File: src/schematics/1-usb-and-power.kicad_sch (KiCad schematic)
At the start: 49 parts, among them Q101 NX6008NBKW, U101 MP5016HGQH, U102 BQ24392RSER, U103 FUSB302BMPX, U104 TPS628512DRLR

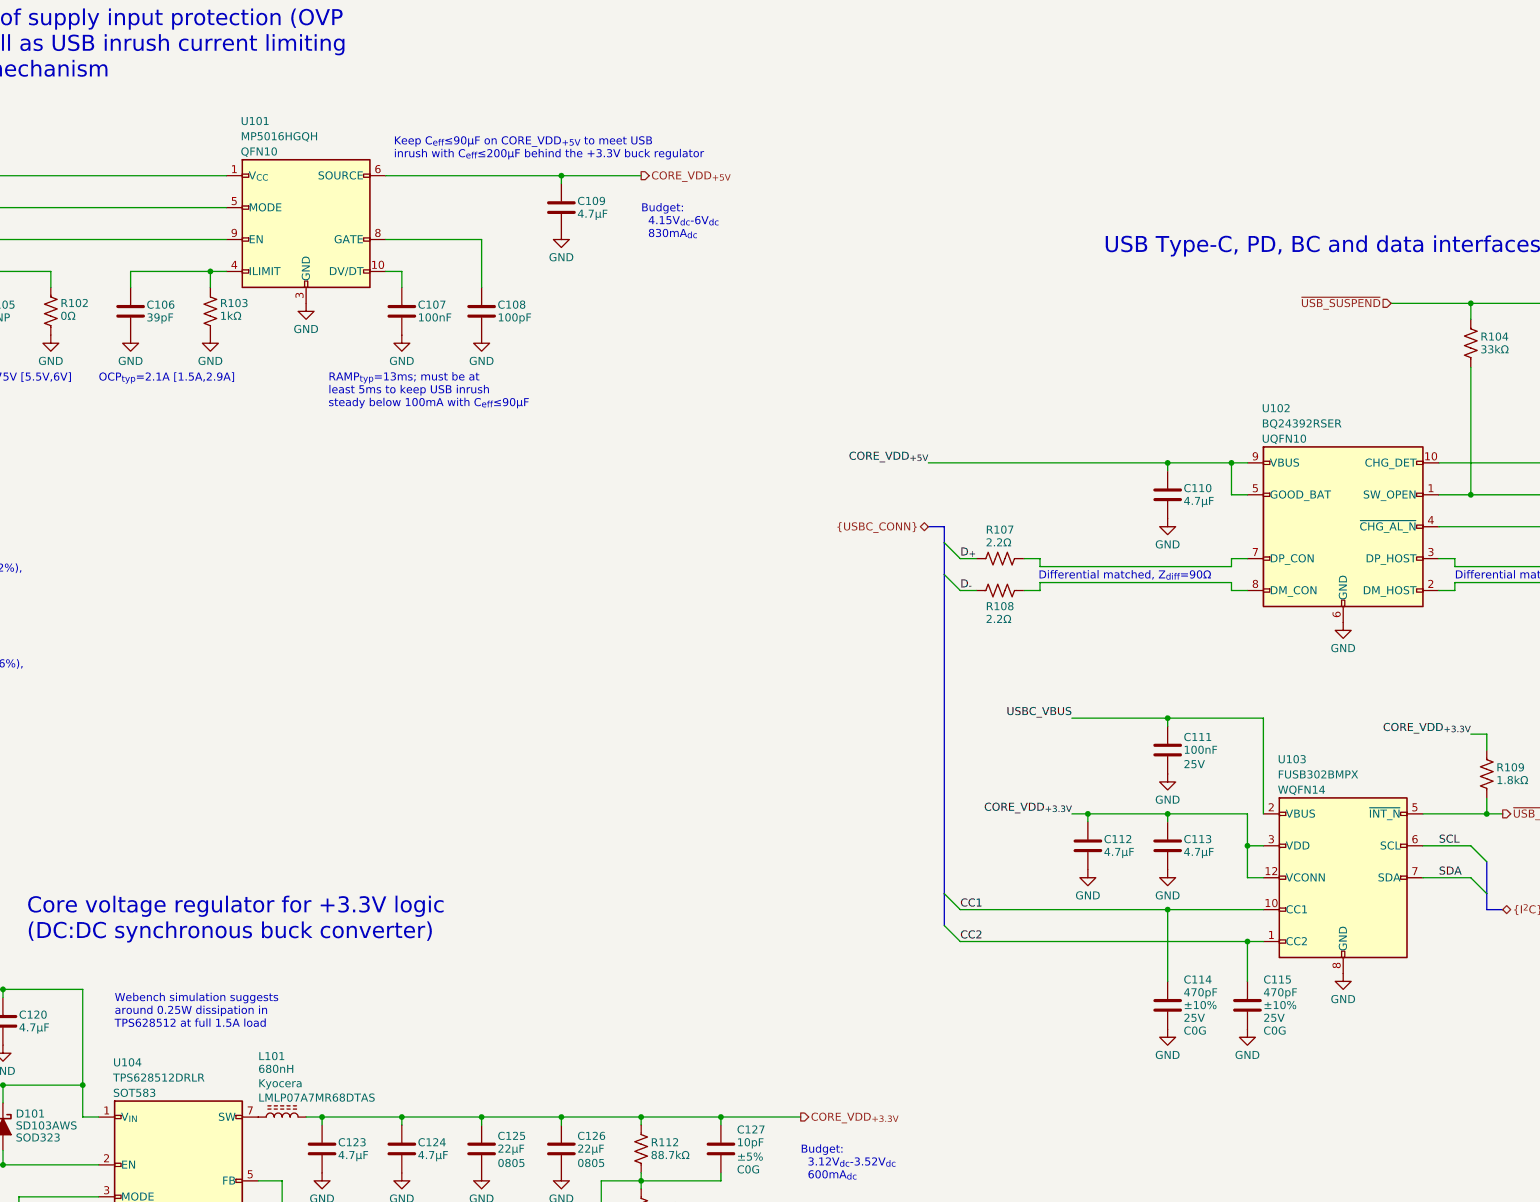
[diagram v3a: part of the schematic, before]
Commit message: Added the I2C address of the FUSB302.
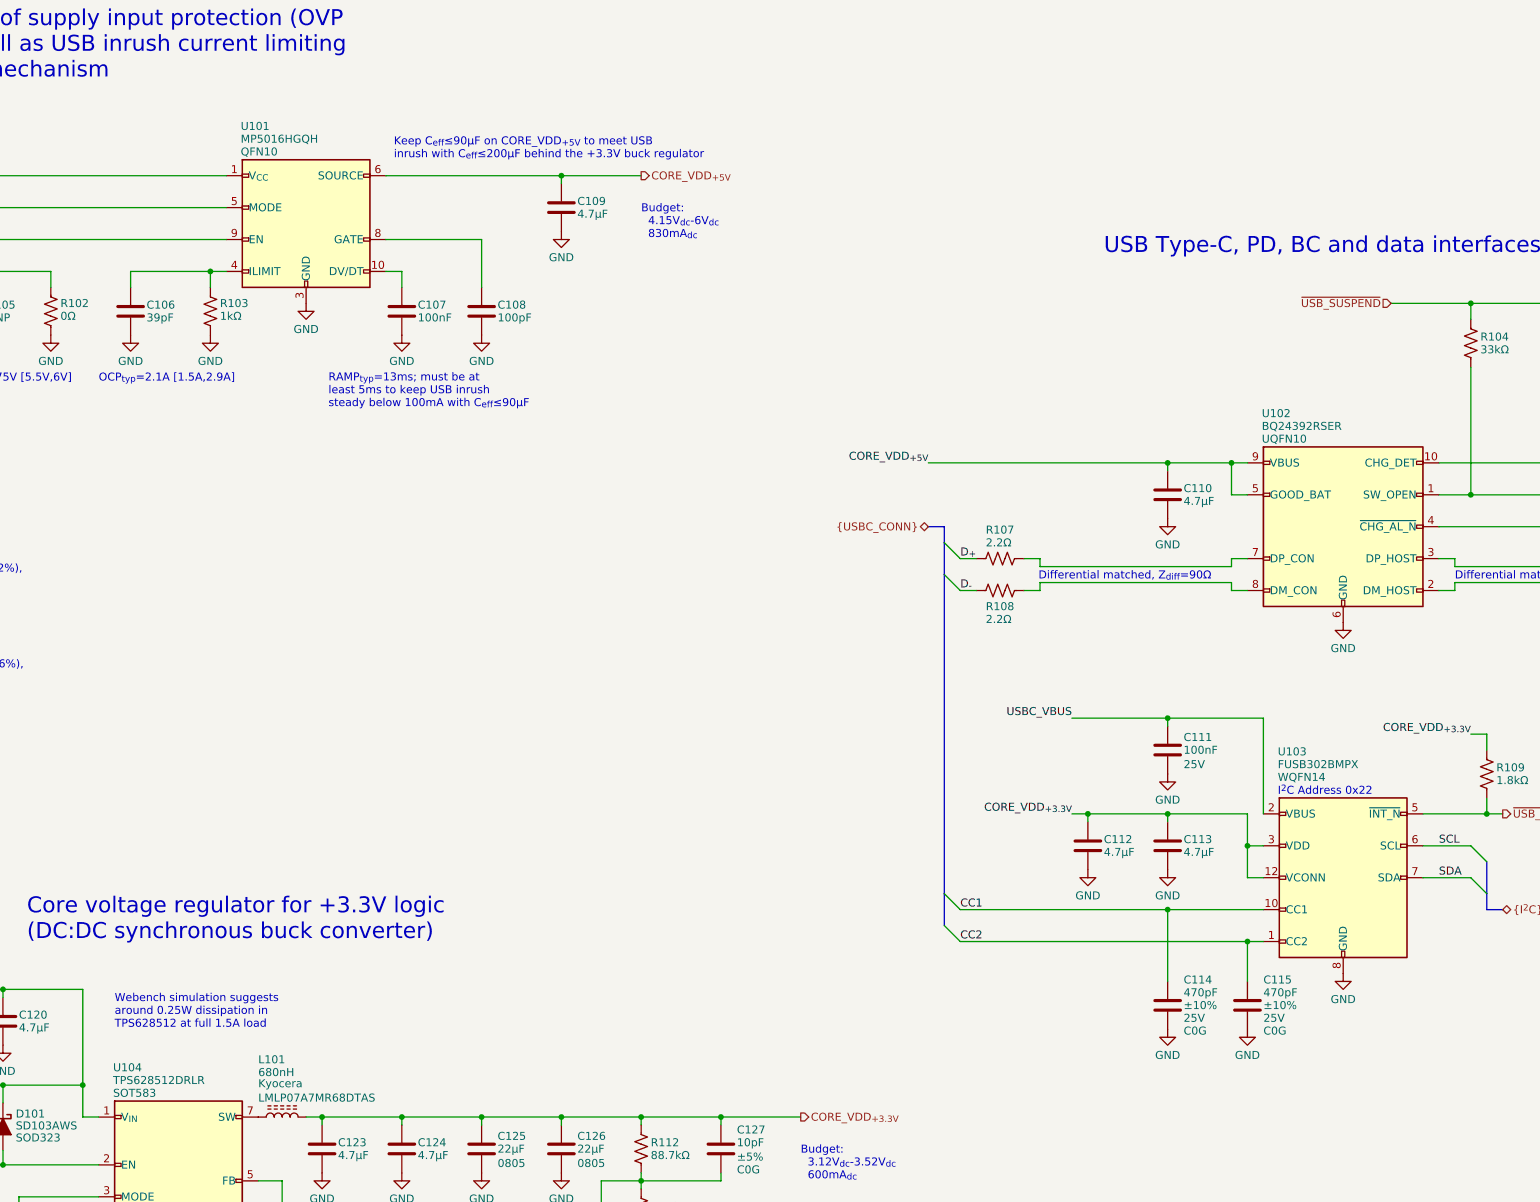
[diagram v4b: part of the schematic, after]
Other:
- note added: "I^{2}C Address 0x22"
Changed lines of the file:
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@@
     (effects (font (size 1.27 1.27)) (justify left bottom))
   )
+  (text "I^{2}C Address 0x22" (at 294.386 162.306 0)
+    (effects (font (size 1.27 1.27)) (justify left bottom))
+  )
   (text "Keep C_{eff}≤90μF on CORE_VDD_{+5V} to meet USB\ninrush with C_{eff}≤200μF behind the +3.3V buck regulator"
     (at 153.67 60.96 0)
@@
   (symbol (lib_id "restall-manufacturer-kyocera:LMLP07A7MR68DTAS") (at 135.89 213.36 90) (unit 1)
     (in_bom yes) (on_board yes) (dnp no)
-    (property "Reference" "L101" (at 132.08 203.708 90)
+    (property "Reference" "L101" (at 132.08 204.216 90)
       (effects (font (size 1.27 1.27)) (justify right))
     )
-    (property "Value" "680nH" (at 132.08 205.74 90)
+    (property "Value" "680nH" (at 132.08 206.248 90)
       (effects (font (size 1.27 1.27)) (justify right))
     )
@@
   (symbol (lib_id "restall-manufacturer-onsemi:FUSB302BMPX") (at 304.8 175.26 0) (unit 1)
     (in_bom yes) (on_board yes) (dnp no)
-    (property "Reference" "U103" (at 294.386 156.4416 0)
+    (property "Reference" "U103" (at 294.386 155.194 0)
       (effects (font (size 1.27 1.27)) (justify left))
     )
-    (property "Value" "FUSB302BMPX" (at 294.386 158.8658 0)
+    (property "Value" "FUSB302BMPX" (at 294.386 157.226 0)
       (effects (font (size 1.27 1.27)) (justify left))
     )
@@
       (effects (font (size 1.27 1.27)) (justify left) hide)
     )
-    (property "Package" "WQFN14" (at 294.386 161.29 0)
+    (property "Package" "WQFN14" (at 294.386 159.258 0)
       (effects (font (size 1.27 1.27)) (justify left))
     )
@@
   (symbol (lib_id "restall-manufacturer-ti:BQ24392RSER") (at 304.8 119.38 0) (unit 1)
     (in_bom yes) (on_board yes) (dnp no)
-    (property "Reference" "U102" (at 291.846 100.5616 0)
+    (property "Reference" "U102" (at 291.846 101.346 0)
       (effects (font (size 1.27 1.27)) (justify left))
     )
-    (property "Value" "BQ24392RSER" (at 291.846 102.9858 0)
+    (property "Value" "BQ24392RSER" (at 291.846 103.378 0)
       (effects (font (size 1.27 1.27)) (justify left))
     )
@@
   (symbol (lib_id "restall-manufacturer-mps:MP5016HGQH") (at 139.7 71.12 0) (unit 1)
     (in_bom yes) (on_board yes) (dnp no)
-    (property "Reference" "U101" (at 129.286 54.8416 0)
+    (property "Reference" "U101" (at 129.286 55.626 0)
       (effects (font (size 1.27 1.27)) (justify left))
     )
-    (property "Value" "MP5016HGQH" (at 129.286 57.2658 0)
+    (property "Value" "MP5016HGQH" (at 129.286 57.658 0)
       (effects (font (size 1.27 1.27)) (justify left))
     )
@@
   (symbol (lib_id "restall-manufacturer-ti:TPS62851?DRLR") (at 119.38 222.25 0) (unit 1)
     (in_bom yes) (on_board yes) (dnp no)
-    (property "Reference" "U104" (at 108.966 204.7016 0)
+    (property "Reference" "U104" (at 108.966 205.486 0)
       (effects (font (size 1.27 1.27)) (justify left))
     )
-    (property "Value" "TPS628512DRLR" (at 108.966 207.1258 0)
+    (property "Value" "TPS628512DRLR" (at 108.966 207.518 0)
       (effects (font (size 1.27 1.27)) (justify left))
     )

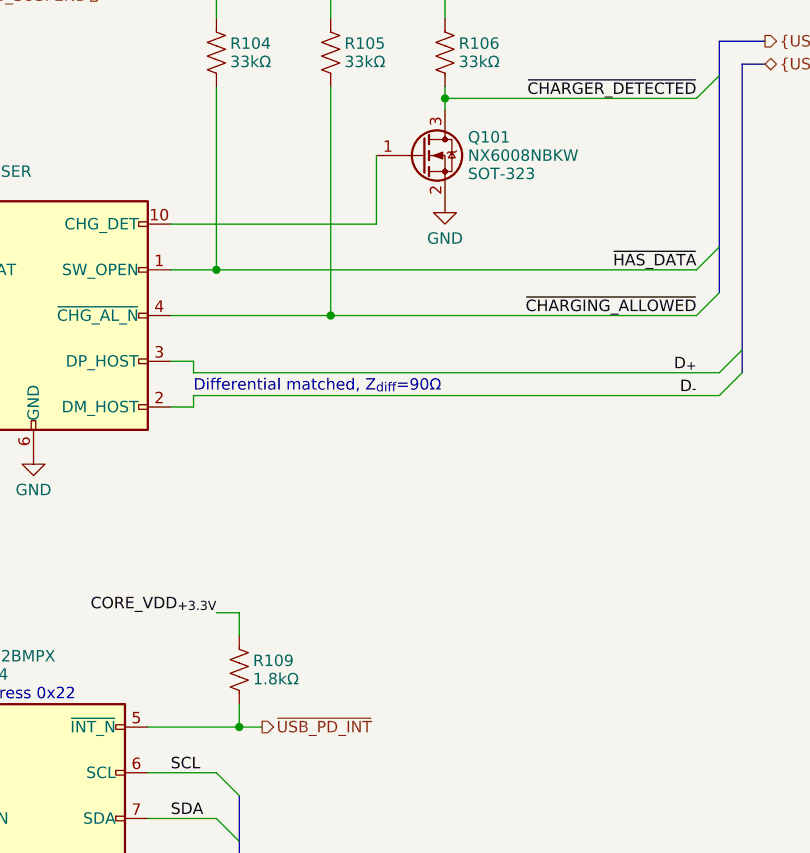
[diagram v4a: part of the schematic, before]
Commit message: Drew the schematic for the sensors.
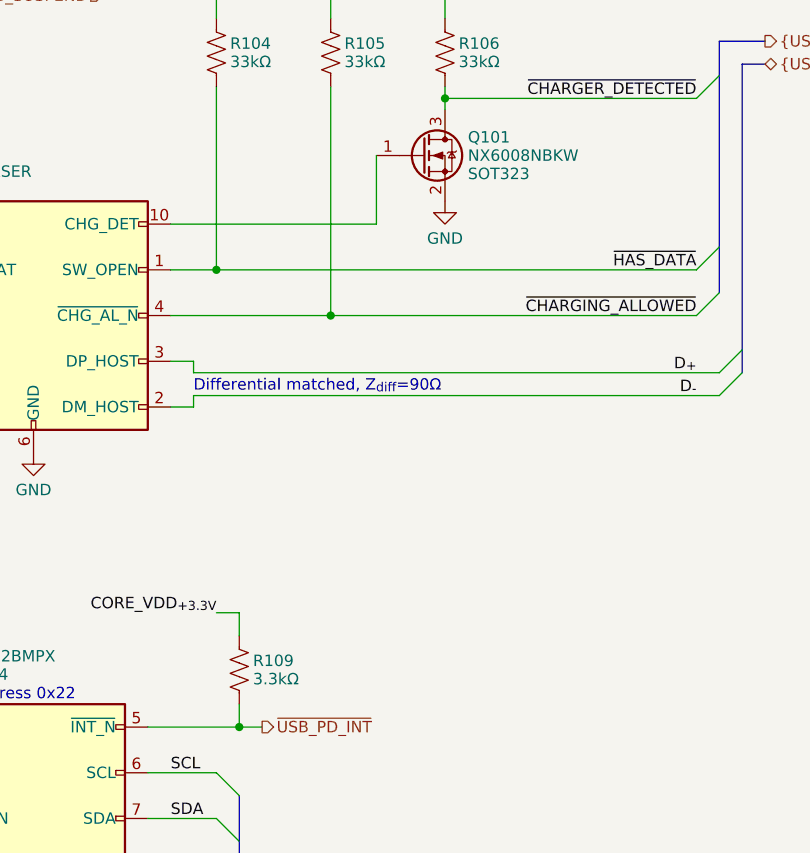
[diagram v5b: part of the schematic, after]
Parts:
- Q101: footprint restall-generic-sot:SOT-323 -> restall-generic-sot:SOT323; Package SOT-323 -> SOT323
- R109: value 1.8kΩ -> 3.3kΩ; Label 1.8kΩ±1% 0.0625W -> 3.3kΩ±1% 0.0625W
- U104: footprint restall-manufacturer-ti:SOT-583-8 -> restall-manufacturer-ti:SOT583
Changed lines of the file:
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@@
       (effects (font (size 1.27 1.27)) (justify left))
     )
-    (property "Footprint" "restall-generic-sot:SOT-323" (at 353.06 98.044 0)
+    (property "Footprint" "restall-generic-sot:SOT323" (at 353.06 98.044 0)
       (effects (font (size 1.27 1.27)) (justify left) hide)
     )
@@
       (effects (font (size 1.27 1.27)) (justify left) hide)
     )
-    (property "Package" "SOT-323" (at 353.06 103.632 0)
+    (property "Package" "SOT323" (at 353.06 103.632 0)
       (effects (font (size 1.27 1.27)) (justify left))
     )
@@
       (effects (font (size 1.27 1.27)) (justify left))
     )
-    (property "Footprint" "restall-manufacturer-ti:SOT-583-8" (at 132.842 234.95 0)
+    (property "Footprint" "restall-manufacturer-ti:SOT583" (at 132.842 234.95 0)
       (effects (font (size 1.27 1.27)) (justify left) hide)
     )
@@
       (effects (font (size 1.27 1.27)) (justify left))
     )
-    (property "Value" "1.8kΩ" (at 329.184 159.766 0)
+    (property "Value" "3.3kΩ" (at 329.184 159.766 0)
       (effects (font (size 1.27 1.27)) (justify left))
     )
@@
       (effects (font (size 1.27 1.27)) (justify left) hide)
     )
-    (property "Label" "1.8kΩ±1% 0.0625W" (at 329.438 160.274 0)
-      (effects (font (size 1.27 1.27)) (justify left) hide)
-    )
+    (property "Label" "3.3kΩ±1% 0.0625W" (at 329.438 160.274 0)
+      (effects (font (size 1.27 1.27)) (justify left) hide)
+    )

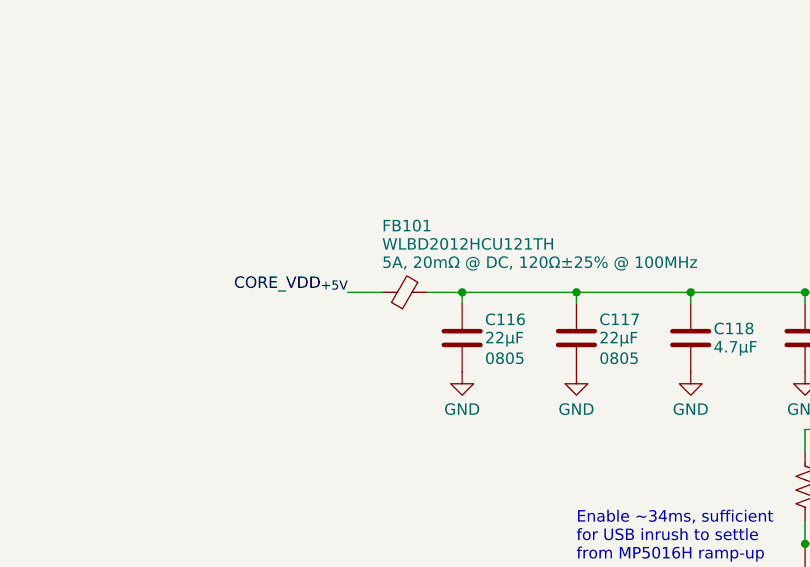
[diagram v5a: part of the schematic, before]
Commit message: Drew the schematic for the TFT driver.
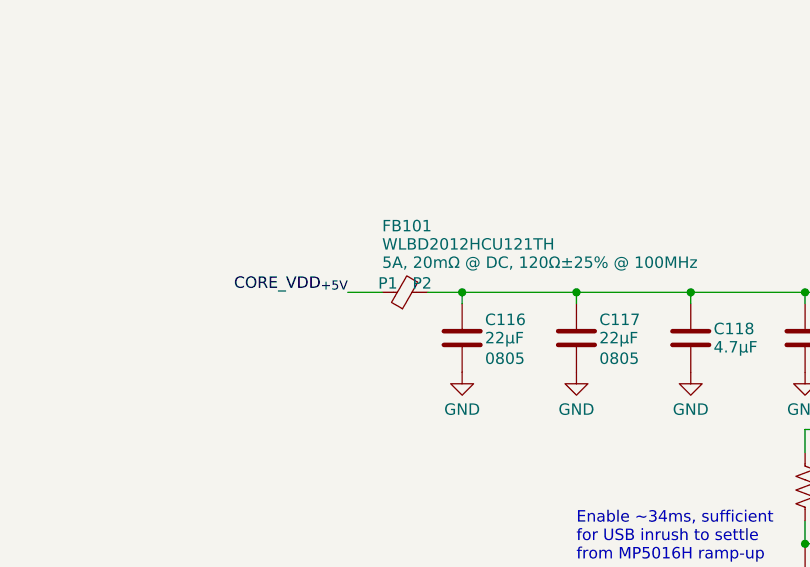
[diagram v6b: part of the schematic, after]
